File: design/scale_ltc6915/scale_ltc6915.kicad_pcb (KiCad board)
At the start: 2 copper layers, 70 x 40 mm, 76 parts, among them J1 USB_B_Micro, J2 Conn_02x03_Odd_Even, J3 Load cell, Q1 IRLML6401, Q2 AO3400, Q3 BC857, SW1 SW_SPST, SW2 ON/OFF switch, U1 MDBT42Q, U2 BQ21040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

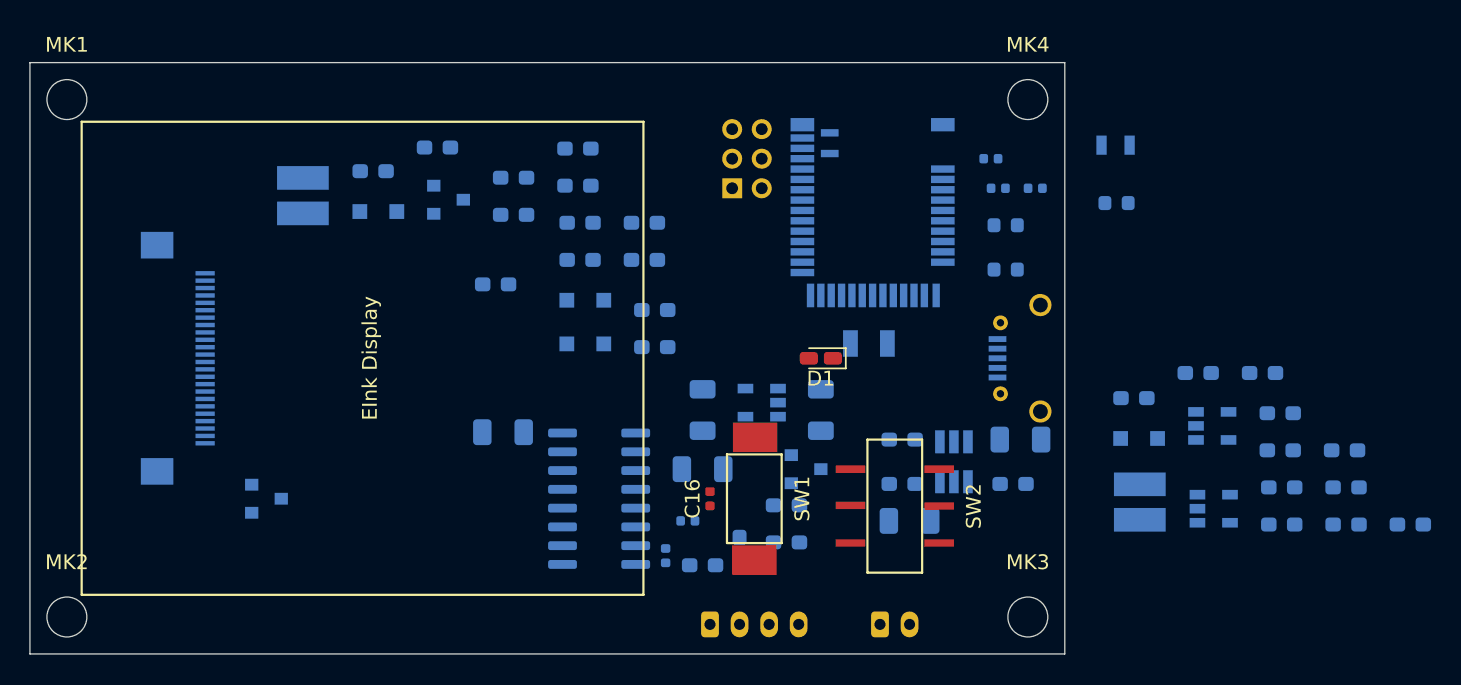
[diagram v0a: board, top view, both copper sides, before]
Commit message: updated schematic of scale_ltc6915, fixed issues
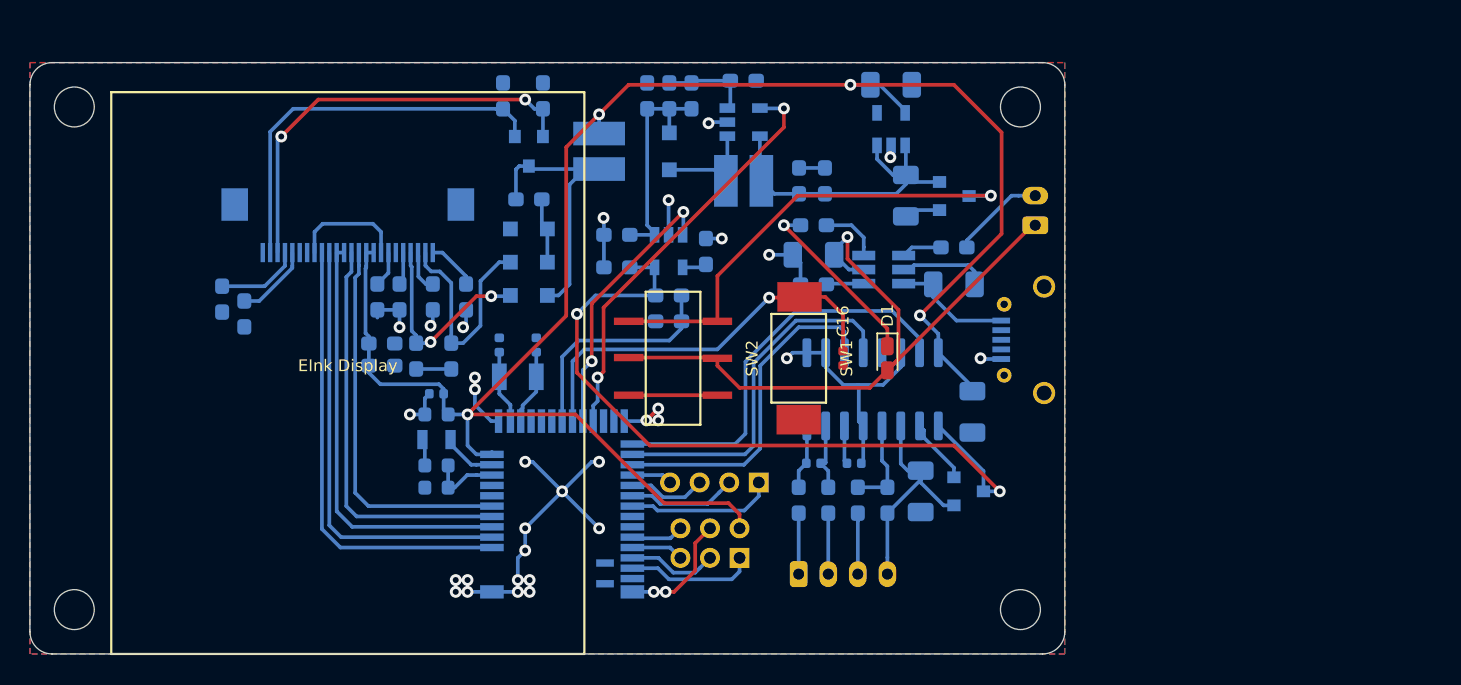
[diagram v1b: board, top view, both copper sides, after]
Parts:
- added J4: Conn_01x04, Connector_PinHeader_2.00mm:PinHeader_1x04_P2.00mm_Vertical, B.Cu at (59.3, 38.4)
- moved C29 55.5 mm to (51.8, 12.2), turned to 90 degrees
- moved R12 52.5 mm to (53.2, 25.8), turned to 180 degrees
- moved C32 51.5 mm to (49.7, 23.9), turned to 180 degrees
- moved L2 50.1 mm to (37.5, 35.5)
- moved L1 49.3 mm to (37.5, 37.2), turned to 180 degrees
- moved C30 48.1 mm to (49.7, 21.6), turned to 180 degrees
- moved Q3 47.5 mm to (73.5, 39.0)
- moved R13 46.5 mm to (53.2, 27.5), turned to 180 degrees
- moved R11 45.2 mm to (54.8, 12.2), turned to 90 degrees
- moved C1 41.2 mm to (37.5, 38.8)
- moved U5 41.2 mm to (58.3, 14.0)
- moved C31 41.1 mm to (55.7, 22.8), turned to 90 degrees
- moved C5 40.7 mm to (37.5, 32.4)
- moved C3 40.6 mm to (37.5, 33.8)
- moved C28 40.4 mm to (53.2, 12.2), turned to 90 degrees
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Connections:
- C8 pad 1: /nRF/VBAT -> /Sheet5E602498/VBAT
- EINK1 pad 10: (no net) -> /Sheet5E60241E/EINK_RST
- EINK1 pad 13: (no net) -> /Sheet5E60241E/EINK_SCLK
- EINK1 pad 14: (no net) -> /Sheet5E60241E/EINK_SDIO
- EINK1 pad 9: (no net) -> /Sheet5E60241E/EINK_BUSY
- J2 pad 2: /nRF/RX -> VDD
- J2 pad 4: VDD -> GND
- J2 pad 5: /nRF/TX -> /nRF/RX
- J2 pad 6: GND -> /nRF/TX
- Q1 pad 2: /nRF/VBAT -> /Sheet5E602498/VBAT
- U1 pad 18: (no net) -> /Sheet5E602498/Vlc
- U1 pad 2: (no net) -> /Sheet5E60241E/EINK_BUSY
- U1 pad 20: (no net) -> /Sheet5E602498/10V_LDO_EN
- U1 pad 21: (no net) -> /Sheet5E602498/BOOST_EN
- U1 pad 25: (no net) -> /Sheet5E602498/HX711_RATE
- U1 pad 26: (no net) -> /Sheet5E602498/HX711_DATA
- U1 pad 27: (no net) -> /Sheet5E602498/HX711_CLK
- U1 pad 28: (no net) -> /nRF/GPIO3
- U1 pad 29: (no net) -> /nRF/GPIO2
- U1 pad 3: (no net) -> /Sheet5E60241E/EINK_RST
- U1 pad 30: (no net) -> /nRF/GPIO1
- U1 pad 31: (no net) -> /nRF/GPIO0
- U1 pad 4: (no net) -> /Sheet5E60241E/EINK_CS
- U1 pad 5: (no net) -> /Sheet5E60241E/EINK_SCLK
- U1 pad 6: (no net) -> /Sheet5E60241E/EINK_SDIO
- U3 pad 1: /nRF/VBAT -> /Sheet5E602498/VBAT
- U3 pad 3: /nRF/VBAT -> /Sheet5E602498/VBAT
- U4 pad 11: (no net) -> /Sheet5E602498/HX711_CLK
- U4 pad 12: (no net) -> /Sheet5E602498/HX711_DATA
- U4 pad 15: (no net) -> /Sheet5E602498/HX711_RATE
- U5 pad 4: (no net) -> /Sheet5E602498/BOOST_EN
- U6 pad 3: (no net) -> /Sheet5E602498/10V_LDO_EN
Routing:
- net VDD: track 0.00 -> 124.7 mm, vias 0 -> 4
- net GND: track 0.00 -> 113.2 mm, vias 0 -> 33
- net /Sheet5E602498/VSUP: track 0.00 -> 52.1 mm, vias 0 -> 2
- net Net-(BT1-Pad1): track 0.00 -> 47.9 mm, vias 0 -> 1
- net Net-(Q1-Pad3): track 0.00 -> 31.3 mm, vias 0 -> 1
- net /Sheet5E60241E/EINK_BUSY: track 0.00 -> 30.7 mm
- net /Sheet5E60241E/EINK_RST: track 0.00 -> 29.8 mm
- net /Sheet5E60241E/EINK_CS: track 0.00 -> 28.9 mm
- net /Sheet5E60241E/RESE: track 0.00 -> 28.8 mm, vias 0 -> 2
- net /Sheet5E602498/BOOST_EN: track 0.00 -> 28.1 mm, vias 0 -> 2
- net /Sheet5E602498/HX711_RATE: track 0.00 -> 27.7 mm
- net /Sheet5E60241E/EINK_SCLK: track 0.00 -> 27.4 mm
- net /nRF/BUTTON: track 0.00 -> 27.1 mm, vias 0 -> 1
- net /Sheet5E60241E/GDR: track 0.00 -> 26.8 mm
- net /Sheet5E60241E/EINK_SDIO: track 0.00 -> 26.0 mm
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- added copper zone on B.Cu, net GND
- added copper zone on F.Cu, net GND
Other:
- outline, holes or cut-outs redrawn
